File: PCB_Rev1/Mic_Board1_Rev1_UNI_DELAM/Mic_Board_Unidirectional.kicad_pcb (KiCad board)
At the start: 2 copper layers, 50.8 x 38.1 mm, 26 parts, among them J1 Conn_01x03_Pin, J2 532610771, U1 OPA1671IDBVR

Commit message: Mounting holes?
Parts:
- added H1: MountingHole, MountingHole:MountingHole_3.2mm_M3, F.Cu at (3.48, 3.48)
- added H2: MountingHole, MountingHole:MountingHole_3.2mm_M3, F.Cu at (3.48, 11.4)
- added H3: MountingHole, MountingHole:MountingHole_3.2mm_M3, F.Cu at (3.48, 19.4)
- added H4: MountingHole, MountingHole:MountingHole_3.2mm_M3, F.Cu at (3.48, 27.3)

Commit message: accidently clicked
hello

Co-Authored-By: Neha Joby <106851456+nehajoby@users.noreply.github.com>
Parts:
- moved J1 3.54 mm to (152.4, 114.5)
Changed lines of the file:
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@@
 	(footprint "Connector_PinHeader_2.54mm:PinHeader_1x03_P2.54mm_Vertical"
 		(layer "F.Cu")
-		(at 151.92 111 90)
+		(at 152.42 114.5 90)
 		(descr "Through hole straight pin header, 1x03, 2.54mm pitch, single row")
 		(tags "Through hole pin header THT 1x03 2.54mm single row")

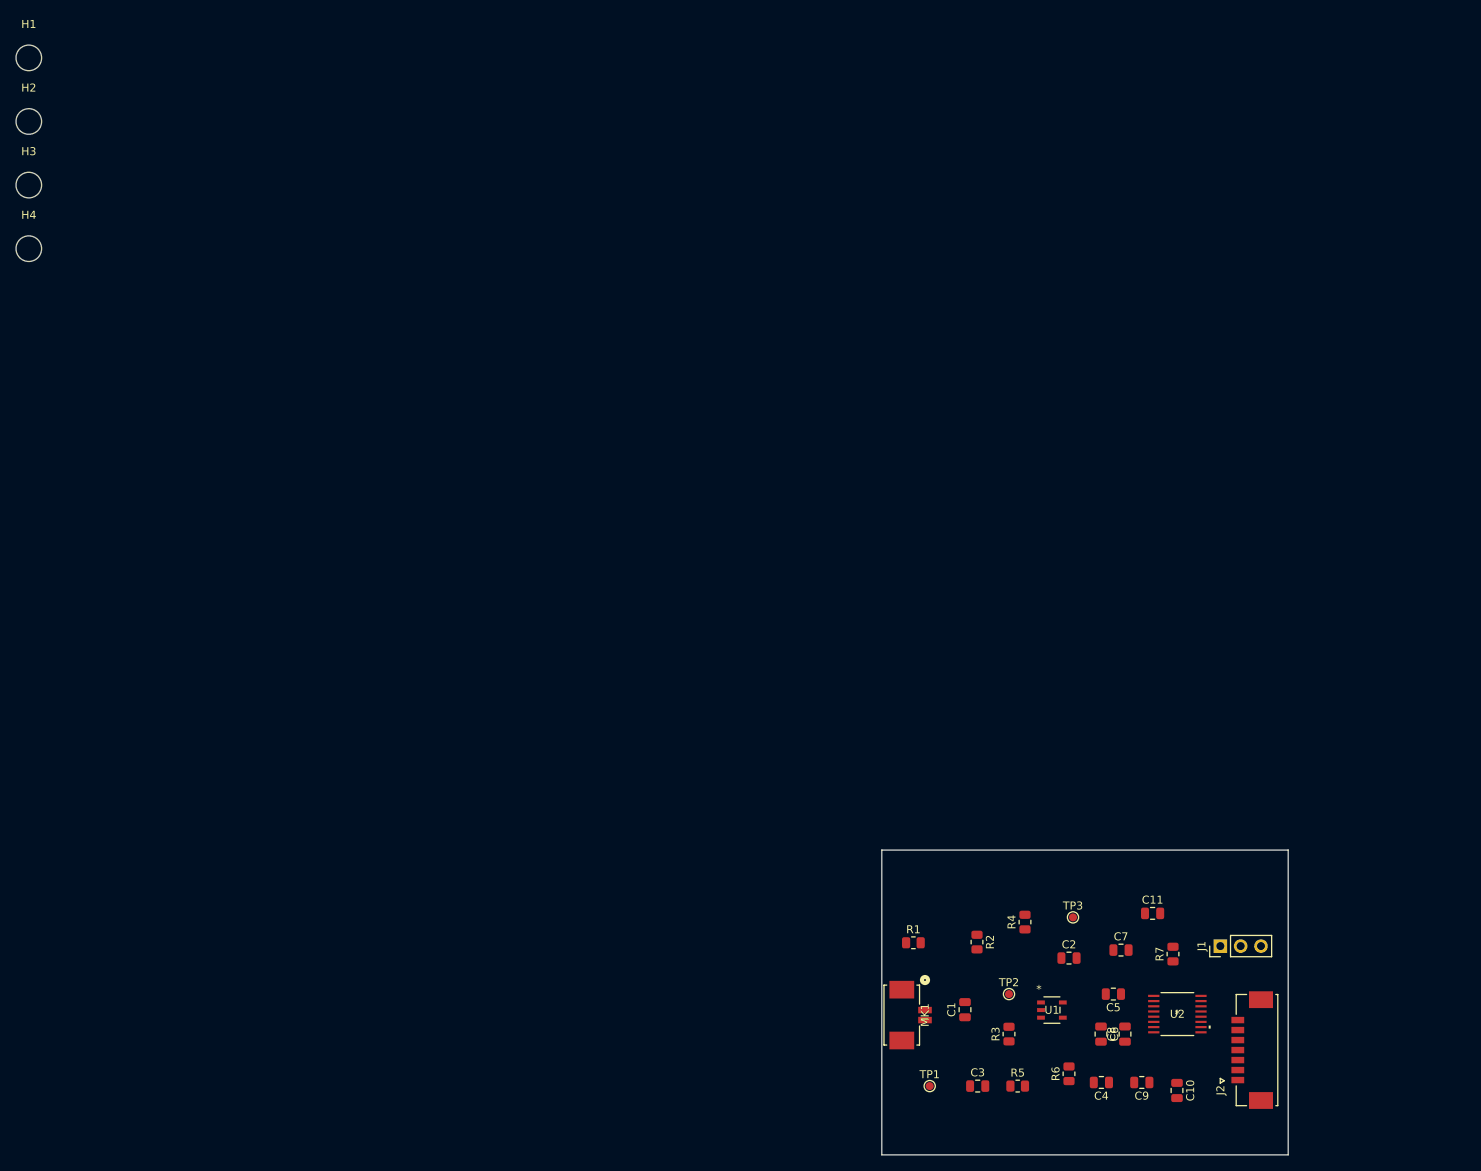
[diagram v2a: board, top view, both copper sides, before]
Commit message: Mic Board Mounting Hole Placement + Fillets + Eliminating Errors
Placed mounting holes, added fillets to the corners of the pcb, and eliminated errors by using correct connector in place of the microphone in the schematic + layout
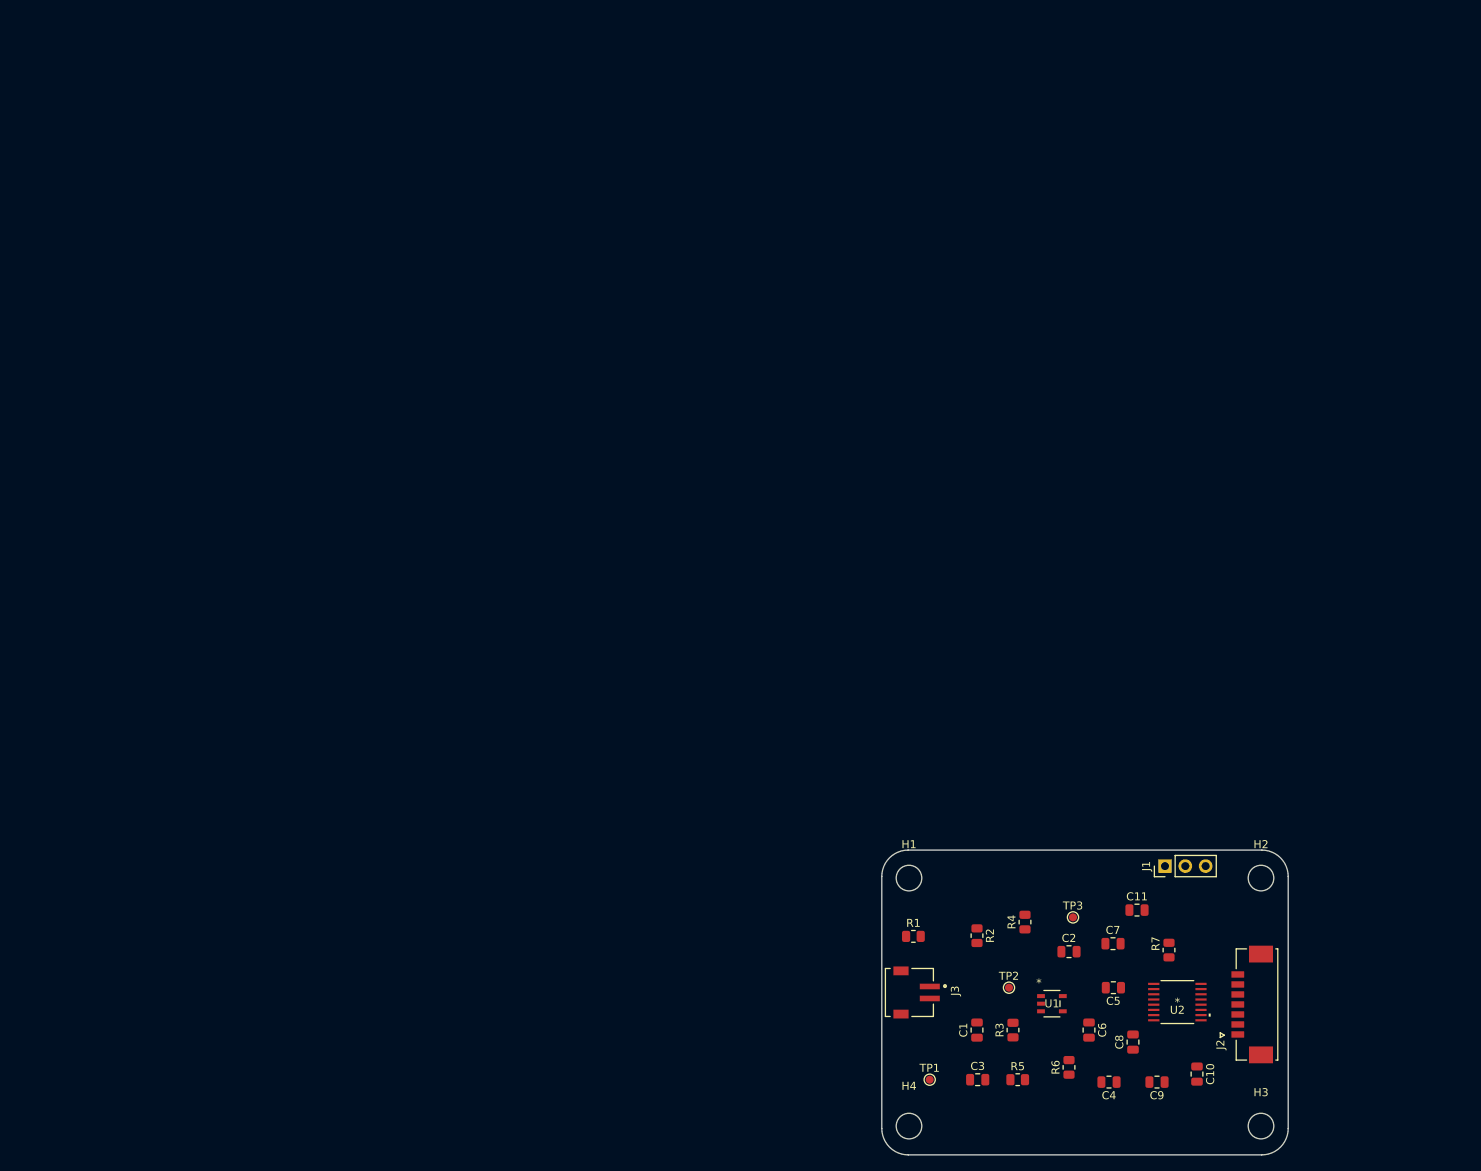
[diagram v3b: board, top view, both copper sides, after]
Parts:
- removed MK1: CMC-97452-L100, Footprints:CONN_532610001-SD_02_MOL
- added J3: S2B-ZR-SM4A-TF_LF__SN_, Footprints:Mic_Conn, F.Cu at (114.0, 120.3)
- moved H3 193.8 mm to (157.5, 137.0)
- moved H2 180.7 mm to (157.5, 106.0)
- moved H4 155.4 mm to (113.5, 137.0)
- moved H1 150.4 mm to (113.5, 106.0)
- moved J1 12.2 mm to (145.5, 104.5)
- moved J2 5.70 mm to (157.0, 121.8)
- moved C10 3.23 mm to (149.5, 130.5)
- moved C1 2.96 mm to (122.0, 125.0)
- moved C11 1.99 mm to (142.0, 110.0)
- moved C9 1.90 mm to (144.5, 131.5)
- moved C6 1.58 mm to (136.0, 125.0)
- moved U2 1.50 mm to (147.0, 121.5)
- moved C8 1.41 mm to (141.5, 126.5)
- moved C7 1.28 mm to (139.0, 114.2)
- moved C4 0.95 mm to (138.5, 131.5)
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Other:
- outline, holes or cut-outs redrawn

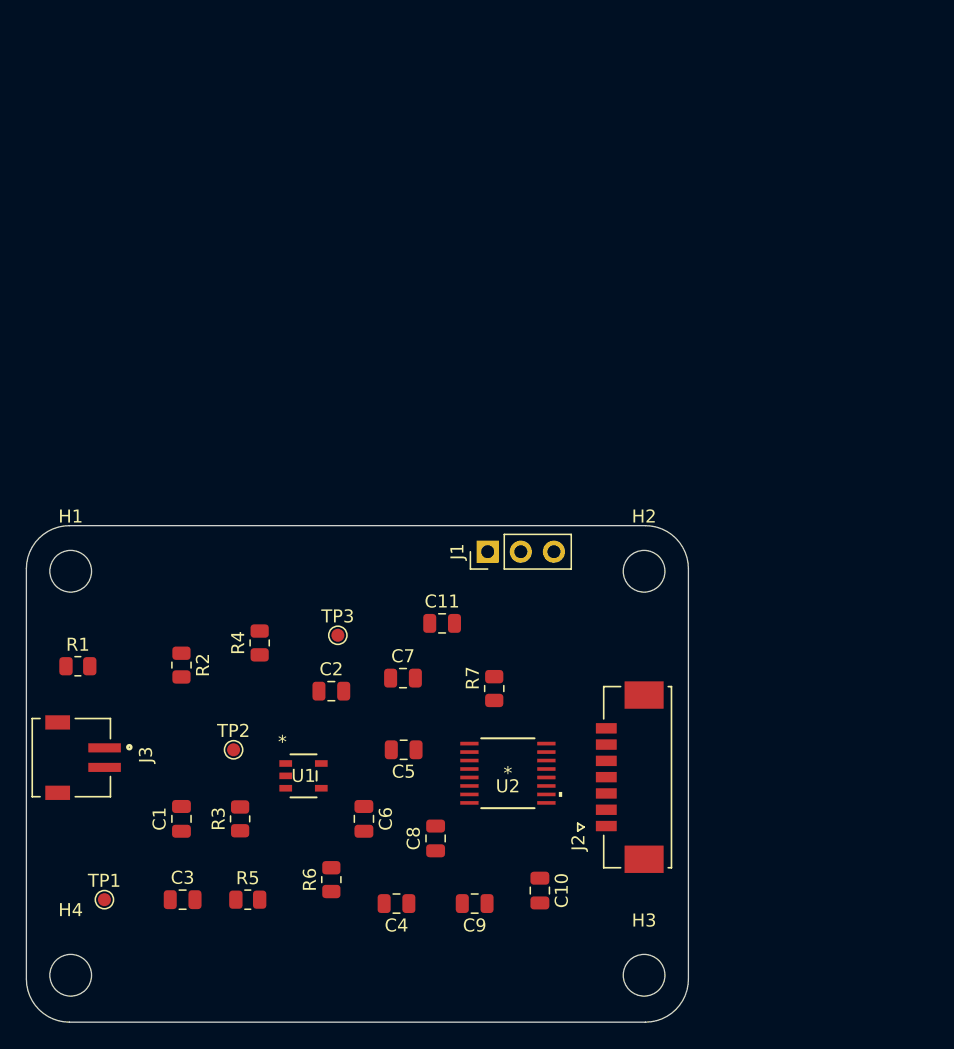
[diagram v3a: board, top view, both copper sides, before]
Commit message: mic board component adjustments
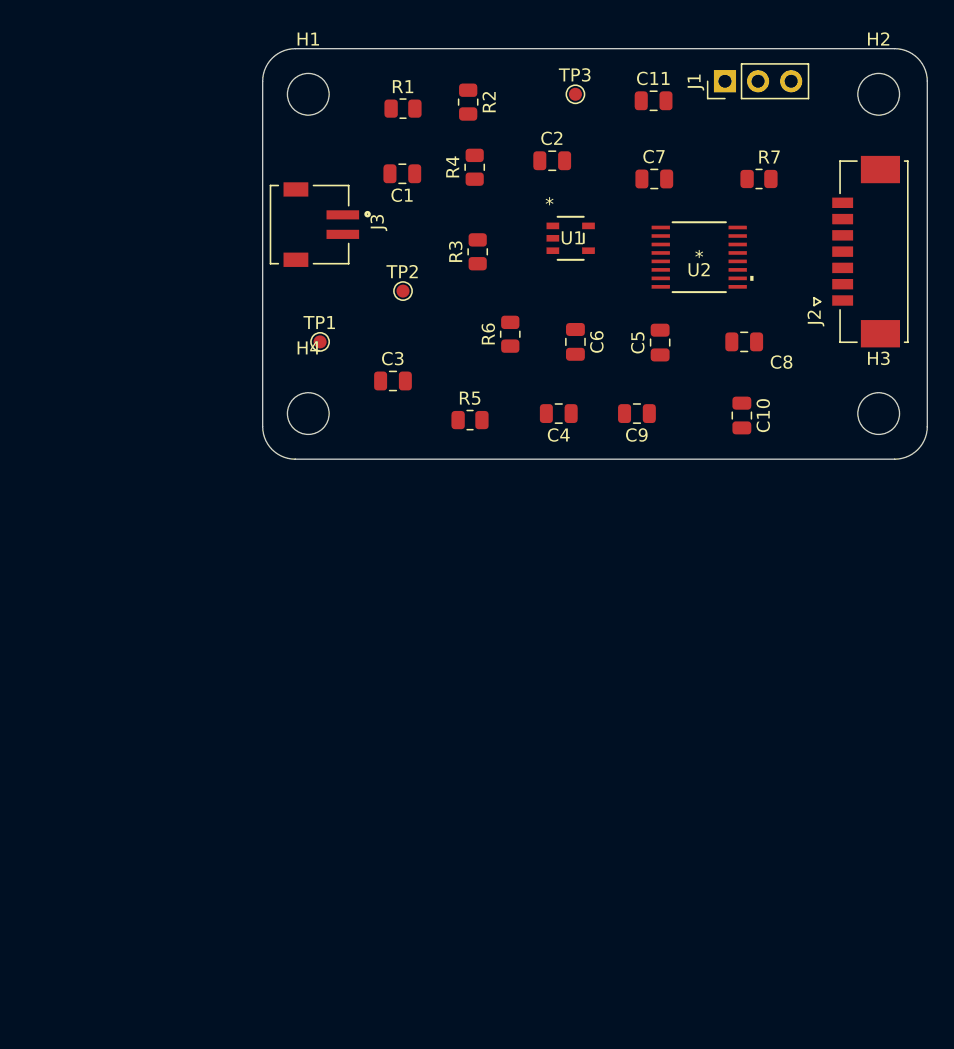
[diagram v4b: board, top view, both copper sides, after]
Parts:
- moved C1 52.3 mm to (138.9, 75.5), turned to 180 degrees
- moved R1 49.5 mm to (139.0, 70.5)
- moved R2 48.5 mm to (144.0, 70.0)
- moved R3 47.2 mm to (144.7, 81.5)
- moved H4 46.8 mm to (131.7, 93.9)
- moved H3 46.7 mm to (175.5, 93.9)
- moved U1 46.1 mm to (151.9, 80.5)
- moved TP1 45.9 mm to (132.6, 88.4)
- moved TP3 45.3 mm to (152.2, 69.4)
- moved C8 44.9 mm to (165.2, 88.4), turned to 180 degrees
- moved J3 44.8 mm to (132.2, 79.4)
- moved J2 44.2 mm to (175.1, 81.5)
- moved C2 44.1 mm to (150.4, 74.5)
- moved R7 44.1 mm to (166.3, 75.9), turned to 0 degrees
- moved R6 44.0 mm to (147.2, 87.8)
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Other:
- board size 50.8 x 38.1 mm -> 51 x 31.5 mm

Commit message: traces
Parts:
- moved C7 0.94 mm to (158.6, 75.0)
- moved R3 0.93 mm to (144.0, 80.9)
- moved TP3 0.27 mm to (152.5, 69.4)
- moved H2 0.10 mm to (175.5, 69.5)
- moved R2 0.09 mm to (144.0, 69.9), turned to 90 degrees
- turned C2 to 180 degrees
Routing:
- net Net-(U1-OUT): track 0.00 -> 42.8 mm, vias 0 -> 8
- net Net-(C2-Pad1): track 0.00 -> 36.7 mm, vias 0 -> 3
- net Net-(U1--IN): track 0.00 -> 34.2 mm, vias 0 -> 6
- net Net-(U2-VCOM): track 0.00 -> 26.0 mm, vias 0 -> 4
- net Net-(U1-+IN): track 0.00 -> 24.5 mm, vias 0 -> 4
- net Net-(C1-Pad1): track 0.00 -> 21.6 mm, vias 0 -> 6
- net Net-(U2-GSEL): track 0.00 -> 16.5 mm
- net Net-(U2-REGO): track 0.00 -> 13.8 mm, vias 0 -> 2
- net Net-(C3-Pad2): track 0.00 -> 12.3 mm, vias 0 -> 2
- net Net-(U2-LIN): track 0.00 -> 12.2 mm, vias 0 -> 4
- net Net-(U2-SDTO): track 0.00 -> 8.49 mm
- net Net-(U2-BICK): track 0.00 -> 8.36 mm
- net Net-(U2-LRCK): track 0.00 -> 8.26 mm
- net Net-(U2-MCLK): track 0.00 -> 8.11 mm
- added copper zone on F.Cu, net +3V3
- added copper zone on B.Cu, net GND

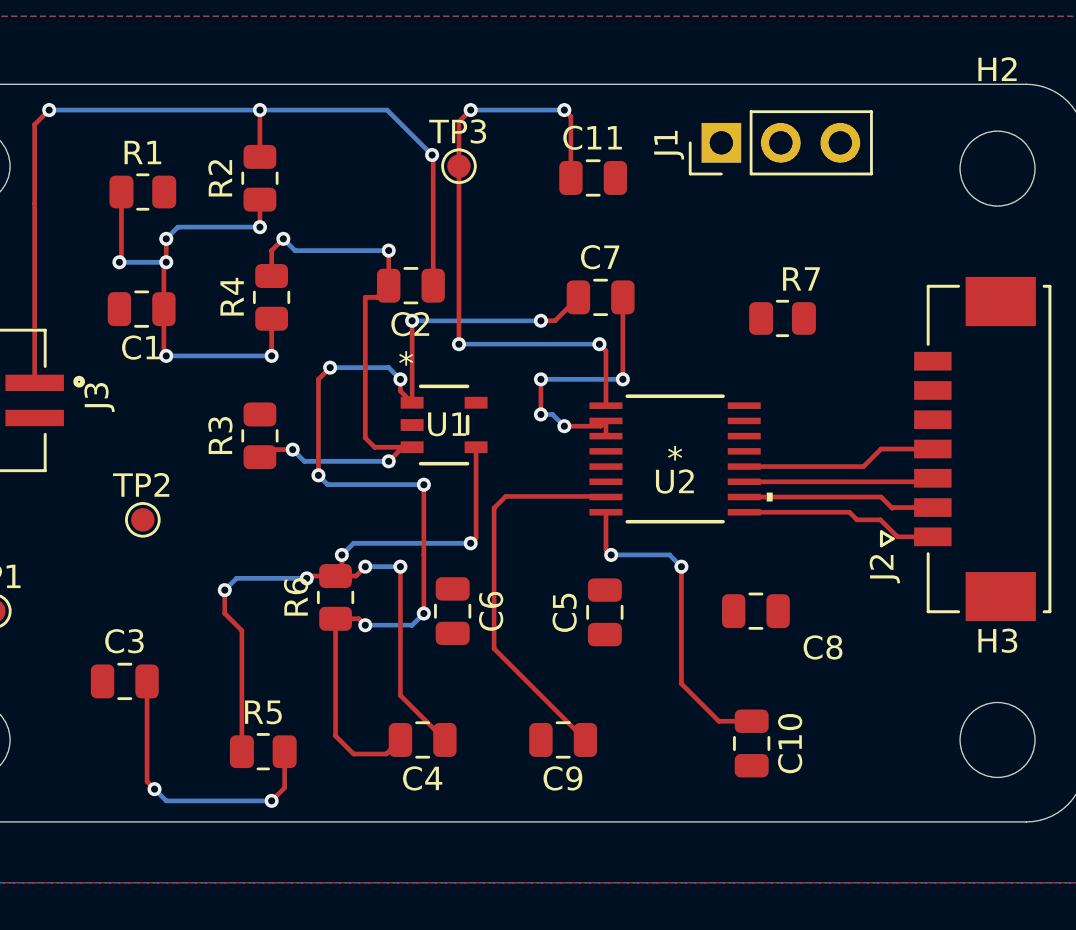
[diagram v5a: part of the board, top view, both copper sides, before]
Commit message: Mic routing
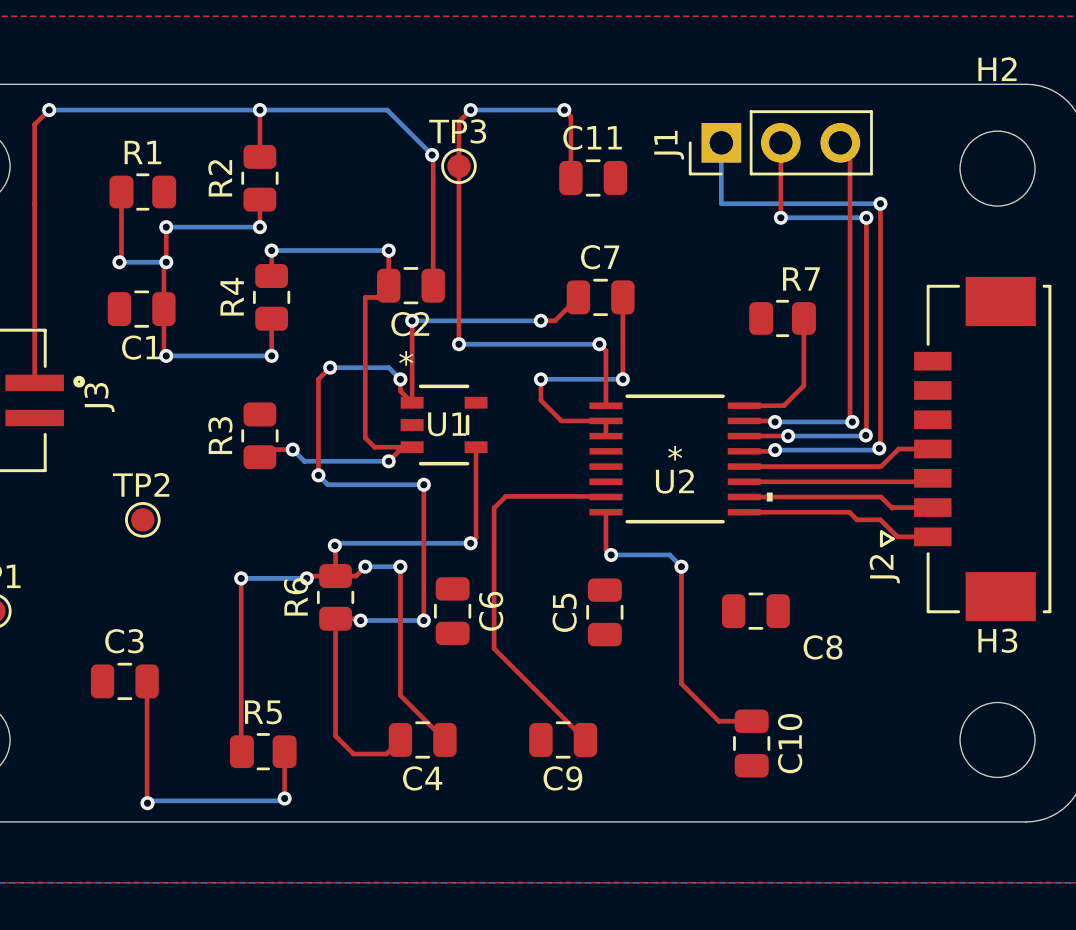
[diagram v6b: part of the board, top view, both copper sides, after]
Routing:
- net Net-(J1-Pin_1): track 0.00 -> 25.8 mm, vias 0 -> 3
- net Net-(J1-Pin_2): track 0.00 -> 21.5 mm, vias 0 -> 4
- net Net-(J1-Pin_3): track 0.00 -> 16.8 mm, vias 0 -> 2
- net Net-(U2-CKS): track 0.00 -> 5.81 mm
- net Net-(C3-Pad2): track 12.3 -> 13.1 mm
- net Net-(U2-LIN): track 12.2 -> 11.7 mm, vias 4 -> 2

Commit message: Routing
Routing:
- net Net-(U2-GSEL): track 16.5 -> 11.9 mm
- net Net-(U1-OUT): track 42.8 -> 41.0 mm
- net Net-(U2-VCOM): track 26.0 -> 24.6 mm
- net Net-(U1--IN): track 34.0 -> 32.7 mm, vias 6 -> 4
- net Net-(C2-Pad1): track 36.7 -> 37.6 mm

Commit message: Micboard Done
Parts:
- moved C6 1.72 mm to (153.6, 89.5), turned to 0 degrees
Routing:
- net GND: track 0.00 -> 144.3 mm, vias 0 -> 16
- net +3V3: track 0.00 -> 68.0 mm, vias 0 -> 15
- net Net-(U1-+IN): track 23.7 -> 31.1 mm
- net Net-(U1-OUT): track 41.0 -> 47.6 mm, vias 8 -> 9
- net Net-(C2-Pad1): track 37.6 -> 36.8 mm
- net Net-(U2-MCLK): track 8.11 -> 8.72 mm, vias 0 -> 2
- net Net-(U2-LRCK): track 8.26 -> 8.59 mm, vias 0 -> 2
- net Net-(U2-SDTO): track 8.49 -> 8.79 mm, vias 0 -> 2
- net Net-(U2-BICK): track 8.36 -> 8.44 mm, vias 0 -> 2
- removed copper zone on F.Cu, net +3V3
- removed copper zone on B.Cu, net GND
